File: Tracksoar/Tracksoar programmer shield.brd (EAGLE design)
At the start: 44 x 19.5 mm, 10 parts, among them U1 FT232RL-BASICSSOP

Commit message: removed old shields
removed square shields and added values to shield passives
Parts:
- C1: value (none) -> 100pf
- C2: value (none) -> 10uf
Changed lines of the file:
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@@
 <element name="LED2" library="adafruit" package="CHIP-LED0805" value="" x="14.0716" y="12.1412" rot="MR0"/>
 <element name="JP2" library="SparkFun-Connectors" package="2X3" value="AVR_SPI_PRG_6PTH" x="42.2148" y="7.4168" rot="R90"/>
-<element name="C1" library="SparkFun-Capacitors" package="0805" value="" x="11.811" y="5.7404" rot="MR270"/>
-<element name="C2" library="SparkFun-Capacitors" package="0805" value="" x="9.7536" y="5.7404" rot="MR270"/>
+<element name="C1" library="SparkFun-Capacitors" package="0805" value="100pf" x="11.811" y="5.7404" rot="MR270"/>
+<element name="C2" library="SparkFun-Capacitors" package="0805" value="10uf" x="9.7536" y="5.7404" rot="MR270"/>
 </elements>
 <signals>

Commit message: test radio build
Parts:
- moved JP2 2.76 mm to (39.5, 7.70), flipped to the bottom
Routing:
- net VCC: track 63.3 -> 71.5 mm
- net SCK: track 30.3 -> 26.4 mm
- net !RESET: track 41.3 -> 37.6 mm
- net MOSI: track 27.6 -> 31.1 mm
- net MISO: track 26.8 -> 24.1 mm
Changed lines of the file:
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@@
 <element name="LED1" library="adafruit" package="CHIP-LED0805" value="" x="10.5156" y="12.0904" rot="MR0"/>
 <element name="LED2" library="adafruit" package="CHIP-LED0805" value="" x="14.0716" y="12.1412" rot="MR0"/>
-<element name="JP2" library="SparkFun-Connectors" package="2X3" value="AVR_SPI_PRG_6PTH" x="42.2148" y="7.4168" rot="R90"/>
+<element name="JP2" library="SparkFun-Connectors" package="2X3" value="AVR_SPI_PRG_6PTH" x="39.4716" y="7.6962" rot="MR90"/>
 <element name="C1" library="SparkFun-Capacitors" package="0805" value="100pf" x="11.811" y="5.7404" rot="MR270"/>
 <element name="C2" library="SparkFun-Capacitors" package="0805" value="10uf" x="9.7536" y="5.7404" rot="MR270"/>
@@
 <wire x1="25.6904" y1="12.3842" x2="25.908" y2="12.1666" width="0.4064" layer="16"/>
 <wire x1="25.908" y1="12.1666" x2="26.0858" y2="11.9888" width="0.4064" layer="16"/>
-<wire x1="26.0858" y1="11.9888" x2="26.0858" y2="8.1534" width="0.4064" layer="16"/>
-<wire x1="26.0858" y1="8.1534" x2="26.0858" y2="5.4356" width="0.4064" layer="16"/>
+<wire x1="26.0858" y1="11.9888" x2="26.0858" y2="10.2108" width="0.4064" layer="16"/>
+<wire x1="26.0858" y1="10.2108" x2="26.0858" y2="5.4356" width="0.4064" layer="16"/>
 <wire x1="26.0858" y1="5.4356" x2="25.654" y2="5.0038" width="0.4064" layer="16"/>
 <wire x1="25.654" y1="5.0038" x2="19.5072" y2="5.0038" width="0.4064" layer="16"/>
@@
 <wire x1="26.0858" y1="16.1036" x2="26.0858" y2="12.1666" width="0.4064" layer="16"/>
 <wire x1="26.0858" y1="12.1666" x2="25.908" y2="12.1666" width="0.4064" layer="16"/>
-<wire x1="39.6748" y1="7.4168" x2="26.8224" y2="7.4168" width="0.4064" layer="16"/>
-<wire x1="26.8224" y1="7.4168" x2="26.0858" y2="8.1534" width="0.4064" layer="16"/>
+<wire x1="42.0116" y1="7.6962" x2="42.4688" y2="7.6962" width="0.3048" layer="16"/>
+<wire x1="42.4688" y1="7.6962" x2="43.307" y2="8.5344" width="0.3048" layer="16"/>
+<wire x1="43.307" y1="8.5344" x2="43.307" y2="11.0236" width="0.3048" layer="16"/>
+<wire x1="43.307" y1="11.0236" x2="42.8244" y2="11.5062" width="0.3048" layer="16"/>
+<wire x1="42.8244" y1="11.5062" x2="27.3812" y2="11.5062" width="0.3048" layer="16"/>
+<wire x1="27.3812" y1="11.5062" x2="26.0858" y2="10.2108" width="0.3048" layer="16"/>
 </signal>
 <signal name="DTR">
@@
 <wire x1="20.1168" y1="3.6576" x2="26.4668" y2="3.6576" width="0.4064" layer="16"/>
 <wire x1="26.4668" y1="3.6576" x2="28.2956" y2="5.4864" width="0.4064" layer="16"/>
-<wire x1="28.2956" y1="5.4864" x2="41.5544" y2="5.4864" width="0.4064" layer="16"/>
-<wire x1="41.5544" y1="5.4864" x2="42.1894" y2="6.1214" width="0.4064" layer="16"/>
-<wire x1="42.1894" y1="6.1214" x2="42.1894" y2="7.3914" width="0.4064" layer="16"/>
-<wire x1="42.1894" y1="7.3914" x2="42.2148" y2="7.4168" width="0.4064" layer="16"/>
+<wire x1="28.2956" y1="5.4864" x2="38.3032" y2="5.4864" width="0.4064" layer="16"/>
+<wire x1="38.3032" y1="5.4864" x2="39.5224" y2="6.7056" width="0.4064" layer="16"/>
+<wire x1="39.5224" y1="6.7056" x2="39.5224" y2="7.6454" width="0.4064" layer="16"/>
+<wire x1="39.5224" y1="7.6454" x2="39.4716" y2="7.6962" width="0.4064" layer="16"/>
 </signal>
 <signal name="MOSI">
 <contactref element="SPI/I2C" pad="5"/>
 <contactref element="JP2" pad="4"/>
-<wire x1="39.6748" y1="9.9568" x2="21.2852" y2="9.9568" width="0.4064" layer="1"/>
 <wire x1="21.6154" y1="1.4954" x2="21.58" y2="1.46" width="0.4064" layer="1"/>
 <wire x1="21.2852" y1="9.9568" x2="20.5994" y2="9.271" width="0.4064" layer="1"/>
@@
 <wire x1="21.59" y1="3.4544" x2="21.59" y2="1.47" width="0.4064" layer="1"/>
 <wire x1="21.59" y1="1.47" x2="21.58" y2="1.46" width="0.4064" layer="1"/>
+<wire x1="42.0116" y1="10.2362" x2="42.0116" y2="9.8806" width="0.3048" layer="1"/>
+<wire x1="42.0116" y1="9.8806" x2="41.148" y2="8.9662" width="0.3048" layer="1"/>
+<wire x1="41.148" y1="8.9662" x2="24.3332" y2="8.9662" width="0.3048" layer="1"/>
+<wire x1="24.3332" y1="8.9662" x2="23.3934" y2="9.9568" width="0.3048" layer="1"/>
+<wire x1="23.3934" y1="9.9568" x2="21.2852" y2="9.9568" width="0.3048" layer="1"/>
 </signal>
 <signal name="SCK">
 <contactref element="SPI/I2C" pad="3"/>
 <contactref element="JP2" pad="3"/>
-<wire x1="42.2148" y1="9.9568" x2="42.0878" y2="9.9568" width="0.3048" layer="16"/>
-<wire x1="42.0878" y1="9.9568" x2="40.9194" y2="8.7884" width="0.3048" layer="16"/>
-<wire x1="40.9194" y1="8.7884" x2="40.9194" y2="6.604" width="0.3048" layer="16"/>
-<wire x1="40.9194" y1="6.604" x2="40.4622" y2="6.1468" width="0.3048" layer="16"/>
-<wire x1="40.4622" y1="6.1468" x2="27.7368" y2="6.1468" width="0.3048" layer="16"/>
-<wire x1="27.7368" y1="6.1468" x2="25.908" y2="4.318" width="0.3048" layer="16"/>
 <wire x1="25.908" y1="4.318" x2="19.685" y2="4.318" width="0.3048" layer="16"/>
 <wire x1="19.685" y1="4.318" x2="18.7198" y2="3.3528" width="0.3048" layer="16"/>
@@
 <wire x1="17.6022" y1="2.8956" x2="17.6022" y2="1.4822" width="0.3048" layer="16"/>
 <wire x1="17.6022" y1="1.4822" x2="17.58" y2="1.46" width="0.3048" layer="16"/>
+<wire x1="39.4716" y1="10.2362" x2="31.8262" y2="10.2362" width="0.3048" layer="16"/>
+<wire x1="31.8262" y1="10.2362" x2="25.908" y2="4.318" width="0.3048" layer="16"/>
 </signal>
 <signal name="SS">
@@
 <contactref element="FTDI" pad="7"/>
 <contactref element="JP2" pad="5"/>
-<wire x1="42.2148" y1="12.4968" x2="42.2148" y2="13.97" width="0.4064" layer="1"/>
-<wire x1="42.2148" y1="13.97" x2="41.7576" y2="14.4272" width="0.4064" layer="1"/>
-<wire x1="41.7576" y1="14.4272" x2="26.797" y2="14.4272" width="0.4064" layer="1"/>
 <wire x1="26.797" y1="14.4272" x2="23.1394" y2="10.7696" width="0.4064" layer="1"/>
 <wire x1="23.1394" y1="10.7696" x2="12.0904" y2="10.7696" width="0.4064" layer="1"/>
@@
 <wire x1="10.7188" y1="12.1412" x2="10.7188" y2="18.1808" width="0.4064" layer="1"/>
 <wire x1="10.7188" y1="18.1808" x2="10.7132" y2="18.1864" width="0.4064" layer="1"/>
+<wire x1="26.797" y1="14.4272" x2="37.8206" y2="14.4272" width="0.4064" layer="1"/>
+<wire x1="37.8206" y1="14.4272" x2="39.4716" y2="12.7762" width="0.4064" layer="1"/>
 </signal>
 <signal name="USBDM">

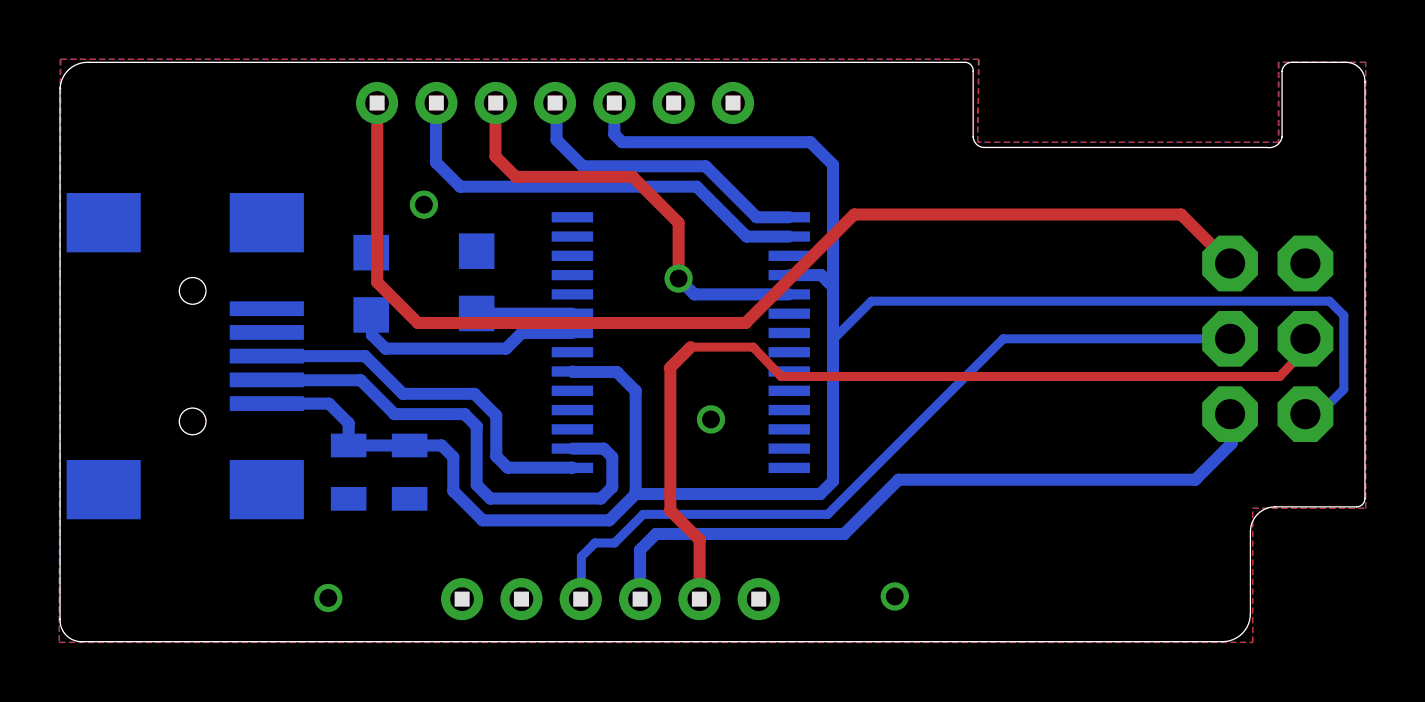
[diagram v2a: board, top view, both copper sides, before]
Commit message: updates
added twometertx-micrf300, changed layout of twometertx, changed led
layout on programmer shield to correct an error, added tracksoar v1.1
to swap power and ground pins on power input header
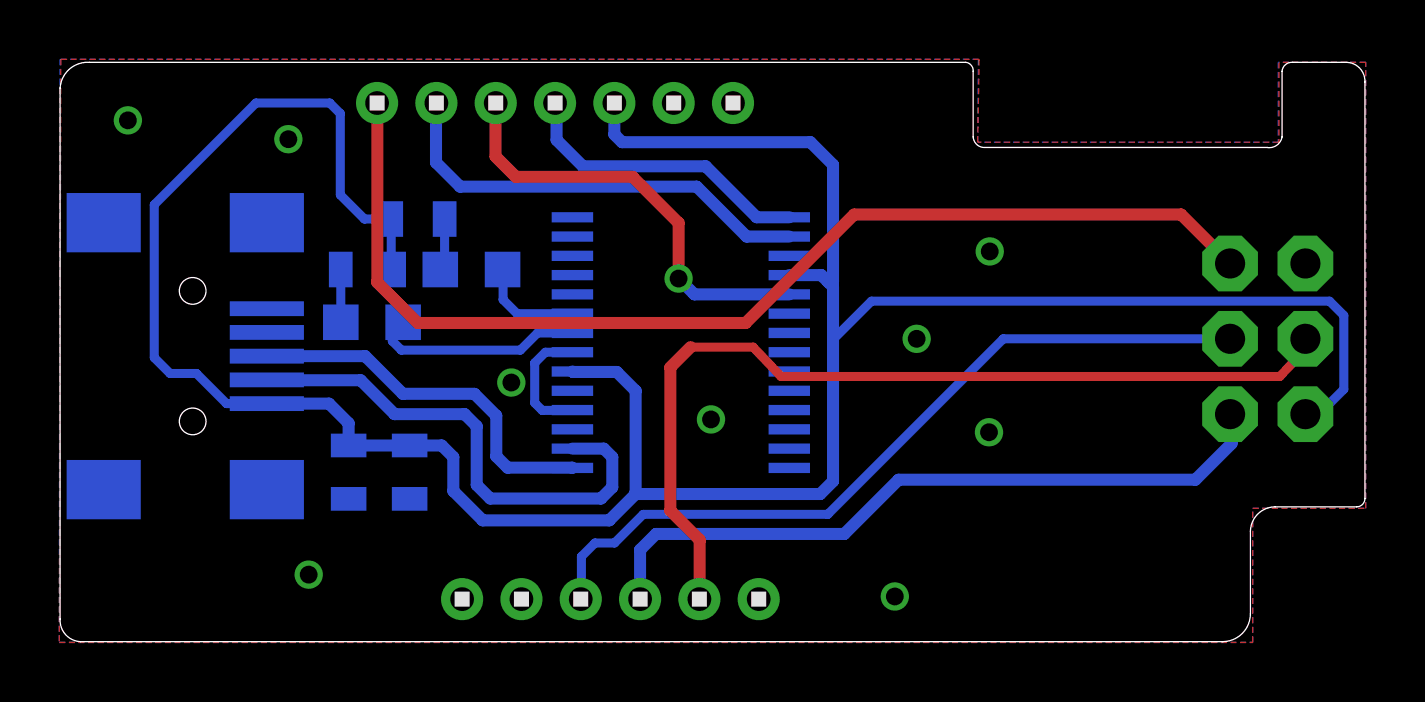
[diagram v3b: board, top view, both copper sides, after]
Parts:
- added R1, R2: (no value), SparkFun-Passives:0805
- moved LED1 1.30 mm to (10.5, 10.8), turned to 90 degrees
- moved LED2 0.47 mm to (13.9, 12.6), turned to 90 degrees
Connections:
- new net N$1: LED2.A, R1.1
- new net N$2: LED1.A, R2.1
- net GND: no longer LED1.C, LED2.C
- net RXLED: now also LED1.C; no longer LED1.A
- net TXLED: now also LED2.C; no longer LED2.A
- net VCC: now also R1.2, R2.2
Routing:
- net VCC: track 71.5 -> 97.6 mm
- net GND: track 0.00 -> 4.15 mm, vias 4 -> 9
- net N$2: track 0.00 -> 1.78 mm
- net N$1: track 0.00 -> 1.76 mm
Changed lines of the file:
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@@
 <?xml version="1.0" encoding="utf-8"?>
 <!DOCTYPE eagle SYSTEM "eagle.dtd">
-<eagle version="7.3.0">
+<eagle version="7.5.0">
 <drawing>
 <settings>
@@
 <layers>
 <layer number="1" name="Top" color="4" fill="1" visible="yes" active="yes"/>
+<layer number="2" name="Route2" color="1" fill="3" visible="yes" active="yes"/>
+<layer number="3" name="Route3" color="4" fill="3" visible="yes" active="yes"/>
+<layer number="14" name="Route14" color="1" fill="6" visible="yes" active="yes"/>
+<layer number="15" name="Route15" color="4" fill="6" visible="yes" active="yes"/>
 <layer number="16" name="Bottom" color="1" fill="1" visible="yes" active="yes"/>
 <layer number="17" name="Pads" color="2" fill="1" visible="yes" active="yes"/>
@@
 </element>
 <element name="U1" library="SparkFun-DigitalIC" package="SSOP28DB" value="FT232RL-BASICSSOP" x="20.955" y="10.1092" rot="MR270"/>
-<element name="LED1" library="adafruit" package="CHIP-LED0805" value="" x="10.5156" y="12.0904" rot="MR0"/>
-<element name="LED2" library="adafruit" package="CHIP-LED0805" value="" x="14.0716" y="12.1412" rot="MR0"/>
+<element name="LED1" library="adafruit" package="CHIP-LED0805" value="" x="10.541" y="10.795" rot="MR90"/>
+<element name="LED2" library="adafruit" package="CHIP-LED0805" value="" x="13.8938" y="12.573" rot="MR90"/>
 <element name="JP2" library="SparkFun-Connectors" package="2X3" value="AVR_SPI_PRG_6PTH" x="39.4716" y="7.6962" rot="MR90"/>
 <element name="C1" library="SparkFun-Capacitors" package="0805" value="100pf" x="11.811" y="5.7404" rot="MR270"/>
 <element name="C2" library="SparkFun-Capacitors" package="0805" value="10uf" x="9.7536" y="5.7404" rot="MR270"/>
+<element name="R1" library="SparkFun-Passives" package="0805" value="" x="12.0904" y="14.2748" rot="MR0"/>
+<element name="R2" library="SparkFun-Passives" package="0805" value="" x="10.3886" y="12.573" rot="MR180"/>
 </elements>
 <signals>
@@
 <contactref element="C2" pad="2"/>
 <contactref element="C1" pad="2"/>
-<contactref element="LED2" pad="C"/>
-<contactref element="LED1" pad="C"/>
 <contactref element="JP1" pad="GND"/>
 <contactref element="JP2" pad="6"/>
@@
 <vertex x="31.0134" y="19.6596"/>
 </polygon>
-<via x="9.0678" y="1.4986" extent="1-16" drill="0.6"/>
+<via x="15.24" y="8.763" extent="1-16" drill="0.6"/>
 <via x="21.971" y="7.5184" extent="1-16" drill="0.6"/>
-<via x="12.2936" y="14.7574" extent="1-16" drill="0.6"/>
+<via x="7.7216" y="16.9672" extent="1-16" drill="0.6"/>
 <via x="28.1686" y="1.5494" extent="1-16" drill="0.6"/>
+<wire x1="17.299" y1="9.7842" x2="16.3882" y2="9.7842" width="0.3048" layer="16"/>
+<wire x1="16.3882" y1="9.7842" x2="16.0274" y2="9.4234" width="0.3048" layer="16"/>
+<wire x1="16.0274" y1="9.4234" x2="16.0274" y2="8.0772" width="0.3048" layer="16"/>
+<wire x1="16.0274" y1="8.0772" x2="16.2814" y2="7.8232" width="0.3048" layer="16"/>
+<wire x1="16.2814" y1="7.8232" x2="17.288" y2="7.8232" width="0.3048" layer="16"/>
+<wire x1="17.288" y1="7.8232" x2="17.299" y2="7.8342" width="0.3048" layer="16"/>
+<via x="8.4074" y="2.286" extent="1-16" drill="0.6"/>
+<via x="2.3114" y="17.6022" extent="1-16" drill="0.6"/>
+<via x="31.369" y="13.1826" extent="1-16" drill="0.6"/>
+<via x="31.3436" y="7.0866" extent="1-16" drill="0.6"/>
+<via x="28.9052" y="10.2362" extent="1-16" drill="0.6"/>
 </signal>
 <signal name="VCC">
@@
 <wire x1="42.8244" y1="11.5062" x2="27.3812" y2="11.5062" width="0.3048" layer="16"/>
 <wire x1="27.3812" y1="11.5062" x2="26.0858" y2="10.2108" width="0.3048" layer="16"/>
+<contactref element="R1" pad="2"/>
+<contactref element="R2" pad="2"/>
+<wire x1="11.1904" y1="14.2748" x2="11.1904" y2="12.6712" width="0.3048" layer="16"/>
+<wire x1="11.1904" y1="12.6712" x2="11.2886" y2="12.573" width="0.3048" layer="16" curve="263.522339"/>
+<wire x1="9.093" y1="8.052" x2="5.6386" y2="8.052" width="0.3048" layer="16"/>
+<wire x1="5.6386" y1="8.052" x2="4.6228" y2="9.0678" width="0.3048" layer="16"/>
+<wire x1="4.6228" y1="9.0678" x2="3.7338" y2="9.0678" width="0.3048" layer="16"/>
+<wire x1="3.7338" y1="9.0678" x2="3.2004" y2="9.6012" width="0.3048" layer="16"/>
+<wire x1="3.2004" y1="9.6012" x2="3.2004" y2="14.7574" width="0.3048" layer="16"/>
+<wire x1="3.2004" y1="14.7574" x2="6.6294" y2="18.1864" width="0.3048" layer="16"/>
+<wire x1="6.6294" y1="18.1864" x2="9.1186" y2="18.1864" width="0.3048" layer="16"/>
+<wire x1="9.1186" y1="18.1864" x2="9.4742" y2="17.8308" width="0.3048" layer="16"/>
+<wire x1="9.4742" y1="17.8308" x2="9.4742" y2="15.0876" width="0.3048" layer="16"/>
+<wire x1="9.4742" y1="15.0876" x2="10.287" y2="14.2748" width="0.3048" layer="16"/>
+<wire x1="10.287" y1="14.2748" x2="11.1904" y2="14.2748" width="0.3048" layer="16"/>
 </signal>
 <signal name="DTR">
@@
 <signal name="TXLED">
 <contactref element="U1" pad="23"/>
-<contactref element="LED2" pad="A"/>
-<wire x1="17.299" y1="11.0842" x2="14.0786" y2="11.0842" width="0.4064" layer="16"/>
-<wire x1="14.0786" y1="11.0842" x2="14.0716" y2="11.0912" width="0.4064" layer="16"/>
+<contactref element="LED2" pad="C"/>
+<wire x1="17.299" y1="11.0842" x2="15.4334" y2="11.0842" width="0.3048" layer="16"/>
+<wire x1="15.4334" y1="11.0842" x2="14.9606" y2="11.557" width="0.3048" layer="16"/>
+<wire x1="14.9606" y1="11.557" x2="14.9606" y2="12.5562" width="0.3048" layer="16"/>
+<wire x1="14.9606" y1="12.5562" x2="14.9438" y2="12.573" width="0.3048" layer="16"/>
 </signal>
 <signal name="RXLED">
 <contactref element="U1" pad="22"/>
+<contactref element="LED1" pad="C"/>
+<wire x1="17.299" y1="10.4342" x2="16.1238" y2="10.4342" width="0.3048" layer="16"/>
+<wire x1="16.1238" y1="10.4342" x2="15.5448" y2="9.8552" width="0.3048" layer="16"/>
+<wire x1="15.5448" y1="9.8552" x2="11.5316" y2="9.8552" width="0.3048" layer="16"/>
+<wire x1="11.5316" y1="9.8552" x2="11.2268" y2="10.16" width="0.3048" layer="16"/>
+<wire x1="11.2268" y1="10.16" x2="11.2268" y2="10.9134" width="0.3048" layer="16"/>
+<wire x1="11.2268" y1="10.9134" x2="11.591" y2="10.795" width="0.3048" layer="16"/>
+</signal>
+<signal name="N$1">
+<contactref element="LED2" pad="A"/>
+<contactref element="R1" pad="1"/>
+<wire x1="12.9904" y1="14.2748" x2="12.9904" y2="12.7196" width="0.3048" layer="16"/>
+<wire x1="12.9904" y1="12.7196" x2="12.8438" y2="12.573" width="0.3048" layer="16"/>
+</signal>
+<signal name="N$2">
 <contactref element="LED1" pad="A"/>
-<wire x1="17.299" y1="10.4342" x2="15.5904" y2="10.4342" width="0.4064" layer="16"/>
-<wire x1="15.5904" y1="10.4342" x2="15.0622" y2="9.906" width="0.4064" layer="16"/>
-<wire x1="15.0622" y1="9.906" x2="10.9982" y2="9.906" width="0.4064" layer="16"/>
-<wire x1="10.9982" y1="9.906" x2="10.541" y2="10.3632" width="0.4064" layer="16"/>
-<wire x1="10.541" y1="10.3632" x2="10.541" y2="11.015" width="0.4064" layer="16"/>
-<wire x1="10.541" y1="11.015" x2="10.5156" y2="11.0404" width="0.4064" layer="16"/>
+<contactref element="R2" pad="1"/>
+<wire x1="9.4886" y1="12.573" x2="9.491" y2="10.795" width="0.3048" layer="16"/>
 </signal>
 </signals>
